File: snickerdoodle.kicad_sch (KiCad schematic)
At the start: 8 parts, among them P2 TFM-115-01-F-D-A, P3 TFM-120-01-F-D-A

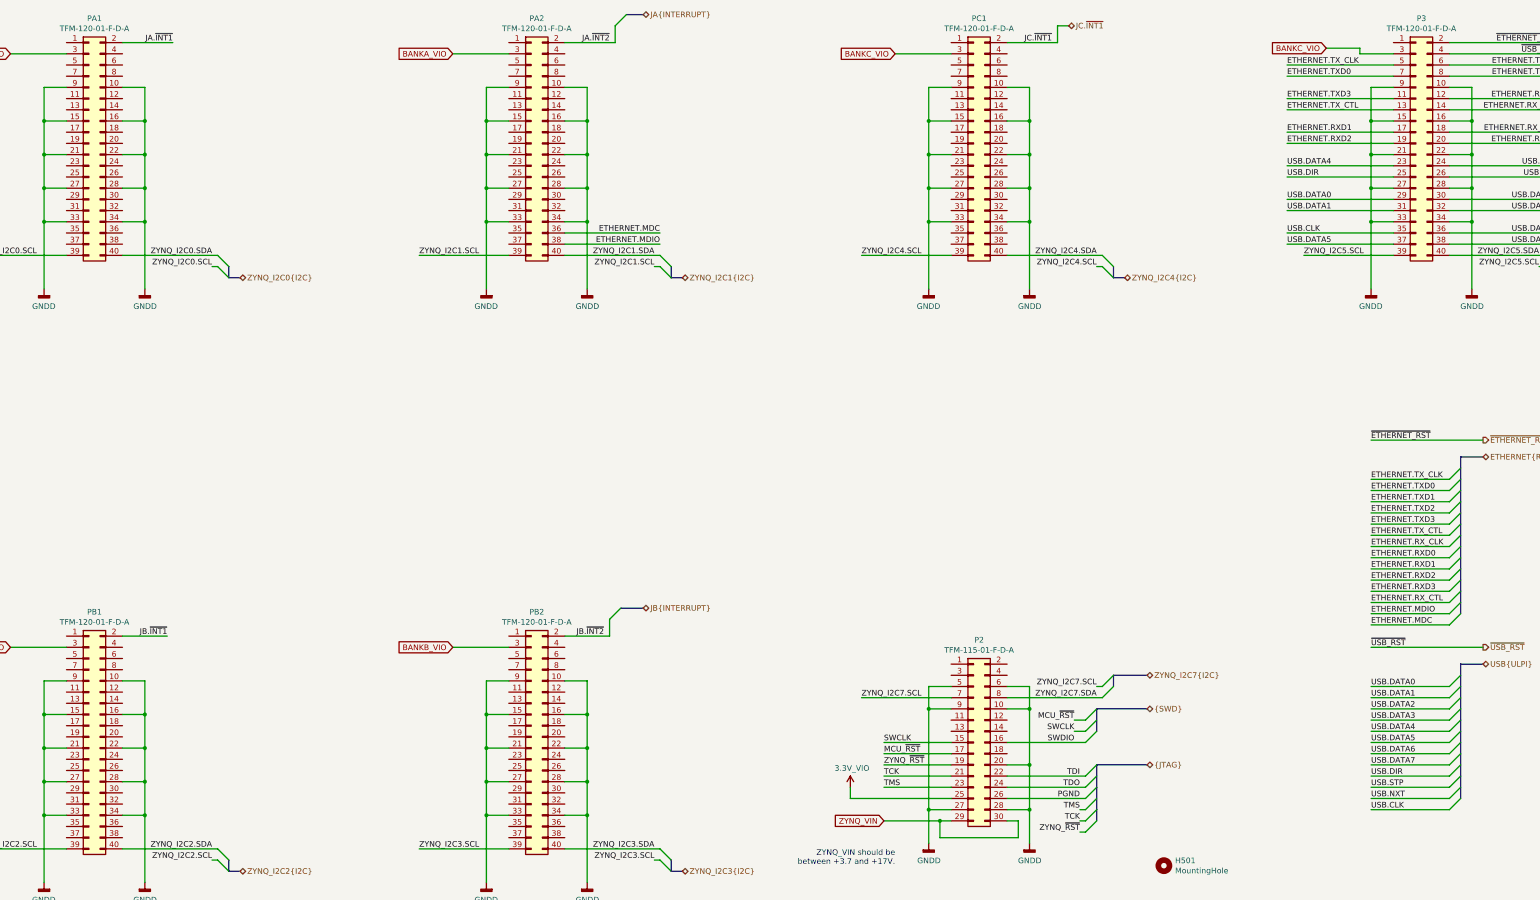
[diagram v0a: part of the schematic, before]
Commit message: Place motor drivers, start layout of Ethernet PHY
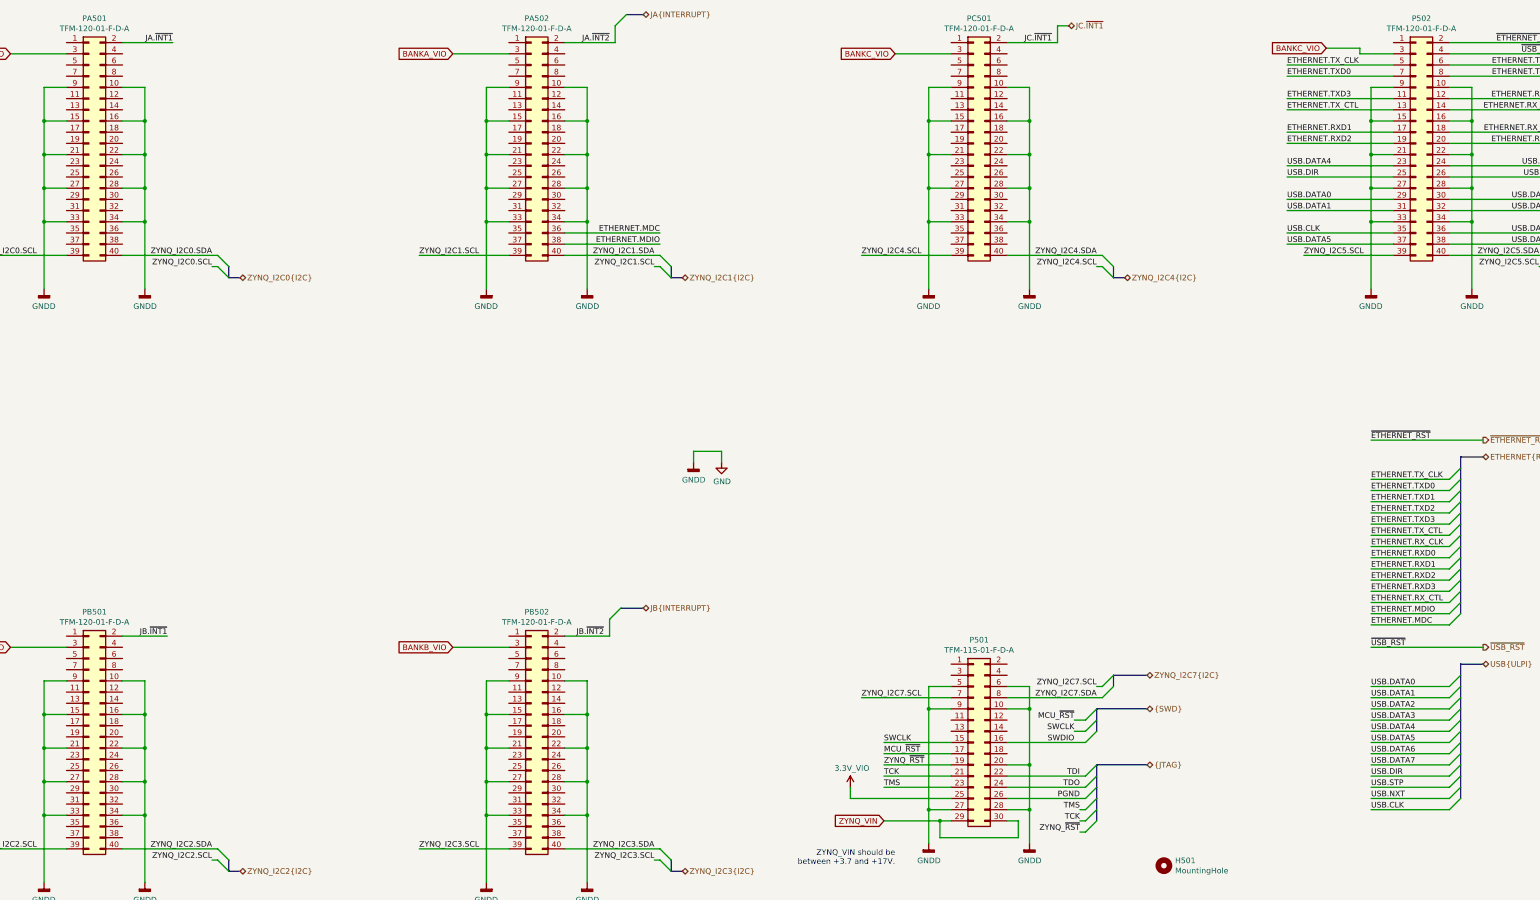
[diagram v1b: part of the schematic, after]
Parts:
- renumbered P2 to P501, P3 to P502, PA1 to PA501, PA2 to PA502, PB1 to PB501, PB2 to PB502, PC1 to PC501
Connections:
- net GNDD renamed GND
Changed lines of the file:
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@@
-(kicad_sch (version 20200618) (host eeschema "5.99.0-unknown-77313e4~101~ubuntu20.04.1")
+(kicad_sch (version 20200618) (host eeschema "5.99.0-unknown-7340c97~102~ubuntu20.04.1")
   (page 5 14)
   (paper "B")
@@
     (comment 1 "Drawn by: Cameron McQuinn")
   )
+  (bus_alias "INTERRUPT" (members "~INT1" "~INT2"))
+  (bus_alias "JTAG" (members "TDI" "TDO" "TCK" "TMS" "ZYNQ_~RST" "PGND"))
+  (bus_alias "I2C" (members "SDA" "SCL"))
   (bus_alias "SWD" (members "MCU_~RST" "SWCLK" "SWDIO"))
-  (bus_alias "I2C" (members "SDA" "SCL"))
-  (bus_alias "JTAG" (members "TDI" "TDO" "TCK" "TMS" "ZYNQ_~RST" "PGND"))
-  (bus_alias "INTERRUPT" (members "~INT1" "~INT2"))
   (junction (at 48.26 45.72) (diameter 0) (color 0 0 0 0))
   (junction (at 48.26 53.34) (diameter 0) (color 0 0 0 0))
@@
     (stroke (width 0) (type solid) (color 0 0 0 0))
   )
+  (wire (pts (xy 195.58 120.65) (xy 195.58 123.19))
+    (stroke (width 0) (type solid) (color 0 0 0 0))
+  )
+  (wire (pts (xy 201.93 120.65) (xy 195.58 120.65))
+    (stroke (width 0) (type solid) (color 0 0 0 0))
+  )
+  (wire (pts (xy 201.93 123.19) (xy 201.93 120.65))
+    (stroke (width 0) (type solid) (color 0 0 0 0))
+  )
   (wire (pts (xy 231.14 196.85) (xy 231.14 199.39))
     (stroke (width 0) (type solid) (color 0 0 0 0))
@@
     (stroke (width 0) (type solid) (color 0 0 0 0))
   )
-  (bus (pts (xy 287.02 196.85) (xy 287.02 201.93))
-    (stroke (width 0) (type solid) (color 0 0 0 0))
-  )
-  (bus (pts (xy 287.02 201.93) (xy 287.02 204.47))
+  (bus (pts (xy 287.02 196.85) (xy 287.02 199.39))
+    (stroke (width 0) (type solid) (color 0 0 0 0))
+  )
+  (bus (pts (xy 287.02 199.39) (xy 287.02 204.47))
     (stroke (width 0) (type solid) (color 0 0 0 0))
   )
@@
     (stroke (width 0) (type solid) (color 0 0 0 0))
   )
-  (bus (pts (xy 369.57 142.24) (xy 369.57 147.32))
-    (stroke (width 0) (type solid) (color 0 0 0 0))
-  )
-  (bus (pts (xy 369.57 147.32) (xy 369.57 152.4))
-    (stroke (width 0) (type solid) (color 0 0 0 0))
-  )
-  (bus (pts (xy 369.57 152.4) (xy 369.57 157.48))
+  (bus (pts (xy 369.57 142.24) (xy 369.57 144.78))
+    (stroke (width 0) (type solid) (color 0 0 0 0))
+  )
+  (bus (pts (xy 369.57 144.78) (xy 369.57 149.86))
+    (stroke (width 0) (type solid) (color 0 0 0 0))
+  )
+  (bus (pts (xy 369.57 149.86) (xy 369.57 154.94))
+    (stroke (width 0) (type solid) (color 0 0 0 0))
+  )
+  (bus (pts (xy 369.57 154.94) (xy 369.57 157.48))
     (stroke (width 0) (type solid) (color 0 0 0 0))
   )
@@
   (symbol (lib_id "Snickerdoodle:3.3V_VIO") (at 231.14 196.85 0) (unit 1)
     (in_bom yes) (on_board yes)
-    (property "Reference" "#PWR0510" (id 0) (at 231.14 200.66 0)
+    (property "Reference" "#PWR0509" (id 0) (at 231.14 200.66 0)
       (effects (font (size 1.27 1.27)) hide)
     )
@@
     )
   )
+  (symbol (lib_id "power:GNDD") (at 195.58 123.19 0) (unit 1)
+    (in_bom yes) (on_board yes)
+    (property "Reference" "#PWR?" (id 0) (at 195.58 129.54 0)
+      (effects (font (size 1.27 1.27)) hide)
+    )
+    (property "Value" "GNDD" (id 1) (at 195.6308 127.1334 0))
+    (property "Footprint" "" (id 2) (at 195.58 123.19 0)
+      (effects (font (size 1.27 1.27)) hide)
+    )
+    (property "Datasheet" "" (id 3) (at 195.58 123.19 0)
+      (effects (font (size 1.27 1.27)) hide)
+    )
+  )
   (symbol (lib_id "power:GNDD") (at 248.92 83.82 0) (mirror y) (unit 1)
     (in_bom yes) (on_board yes)
-    (property "Reference" "#PWR0509" (id 0) (at 248.92 90.17 0)
+    (property "Reference" "#PWR0510" (id 0) (at 248.92 90.17 0)
       (effects (font (size 1.27 1.27)) hide)
     )
@@
   (symbol (lib_id "power:GNDD") (at 248.92 209.55 0) (unit 1)
     (in_bom yes) (on_board yes)
-    (property "Reference" "#PWR0512" (id 0) (at 248.92 215.9 0)
+    (property "Reference" "#PWR0511" (id 0) (at 248.92 215.9 0)
       (effects (font (size 1.27 1.27)) hide)
     )
@@
   (symbol (lib_id "power:GNDD") (at 271.78 83.82 0) (unit 1)
     (in_bom yes) (on_board yes)
-    (property "Reference" "#PWR0511" (id 0) (at 271.78 90.17 0)
+    (property "Reference" "#PWR0512" (id 0) (at 271.78 90.17 0)
       (effects (font (size 1.27 1.27)) hide)
     )
@@
     )
   )
+  (symbol (lib_id "power:GND") (at 201.93 123.19 0) (unit 1)
+    (in_bom yes) (on_board yes)
+    (property "Reference" "#PWR?" (id 0) (at 201.93 129.54 0)
+      (effects (font (size 1.27 1.27)) hide)
+    )
+    (property "Value" "GND" (id 1) (at 202.0443 127.5144 0))
+    (property "Footprint" "" (id 2) (at 201.93 123.19 0)
+      (effects (font (size 1.27 1.27)) hide)
+    )
+    (property "Datasheet" "" (id 3) (at 201.93 123.19 0)
+      (effects (font (size 1.27 1.27)) hide)
+    )
+  )
   (symbol (lib_id "Mechanical:MountingHole") (at 302.26 214.63 0) (unit 1)
     (in_bom yes) (on_board yes)
@@
   (symbol (lib_id "Connector_Generic:Conn_02x15_Odd_Even") (at 259.08 186.69 0) (unit 1)
     (in_bom yes) (on_board yes)
-    (property "Reference" "P2" (id 0) (at 260.35 163.4298 0))
+    (property "Reference" "P501" (id 0) (at 260.35 163.4298 0))
     (property "Value" "TFM-115-01-F-D-A" (id 1) (at 260.35 165.7285 0))
     (property "Footprint" "Connector_Samtec_TFM:Samtec_TFM-115-01-F-D-A_2x15_P1.27mm_Horizontal" (id 2) (at 259.08 186.69 0)
@@
   (symbol (lib_id "Connector_Generic:Conn_02x20_Odd_Even") (at 58.42 50.8 0) (unit 1)
     (in_bom yes) (on_board yes)
-    (property "Reference" "PA1" (id 0) (at 59.69 22.46 0))
+    (property "Reference" "PA501" (id 0) (at 59.69 22.46 0))
     (property "Value" "TFM-120-01-F-D-A" (id 1) (at 59.69 24.7585 0))
     (property "Footprint" "Connector_Samtec_TFM:Samtec_TFM-120-01-F-D-A_2x20_P1.27mm_Horizontal" (id 2) (at 58.42 50.8 0)
@@
   (symbol (lib_id "Connector_Generic:Conn_02x20_Odd_Even") (at 58.42 185.42 0) (unit 1)
     (in_bom yes) (on_board yes)
-    (property "Reference" "PB1" (id 0) (at 59.69 157.08 0))
+    (property "Reference" "PB501" (id 0) (at 59.69 157.08 0))
     (property "Value" "TFM-120-01-F-D-A" (id 1) (at 59.69 159.3785 0))
     (property "Footprint" "Connector_Samtec_TFM:Samtec_TFM-120-01-F-D-A_2x20_P1.27mm_Horizontal" (id 2) (at 58.42 185.42 0)
@@
   (symbol (lib_id "Connector_Generic:Conn_02x20_Odd_Even") (at 158.75 50.8 0) (unit 1)
     (in_bom yes) (on_board yes)
-    (property "Reference" "PA2" (id 0) (at 160.02 22.46 0))
+    (property "Reference" "PA502" (id 0) (at 160.02 22.46 0))
     (property "Value" "TFM-120-01-F-D-A" (id 1) (at 160.02 24.7585 0))
     (property "Footprint" "Connector_Samtec_TFM:Samtec_TFM-120-01-F-D-A_2x20_P1.27mm_Horizontal" (id 2) (at 158.75 50.8 0)
@@
   (symbol (lib_id "Connector_Generic:Conn_02x20_Odd_Even") (at 158.75 185.42 0) (unit 1)
     (in_bom yes) (on_board yes)
-    (property "Reference" "PB2" (id 0) (at 160.02 157.08 0))
+    (property "Reference" "PB502" (id 0) (at 160.02 157.08 0))
     (property "Value" "TFM-120-01-F-D-A" (id 1) (at 160.02 159.3785 0))
     (property "Footprint" "Connector_Samtec_TFM:Samtec_TFM-120-01-F-D-A_2x20_P1.27mm_Horizontal" (id 2) (at 158.75 185.42 0)
@@
   (symbol (lib_id "Connector_Generic:Conn_02x20_Odd_Even") (at 259.08 50.8 0) (unit 1)
     (in_bom yes) (on_board yes)
-    (property "Reference" "PC1" (id 0) (at 260.35 22.46 0))
+    (property "Reference" "PC501" (id 0) (at 260.35 22.46 0))
     (property "Value" "TFM-120-01-F-D-A" (id 1) (at 260.35 24.7585 0))
     (property "Footprint" "Connector_Samtec_TFM:Samtec_TFM-120-01-F-D-A_2x20_P1.27mm_Horizontal" (id 2) (at 259.08 50.8 0)
@@
   (symbol (lib_id "Connector_Generic:Conn_02x20_Odd_Even") (at 359.41 50.8 0) (unit 1)
     (in_bom yes) (on_board yes)
-    (property "Reference" "P3" (id 0) (at 360.68 22.46 0))
+    (property "Reference" "P502" (id 0) (at 360.68 22.46 0))
     (property "Value" "TFM-120-01-F-D-A" (id 1) (at 360.68 24.7585 0))
     (property "Footprint" "Connector_Samtec_TFM:Samtec_TFM-120-01-F-D-A_2x20_P1.27mm_Horizontal" (id 2) (at 359.41 50.8 0)

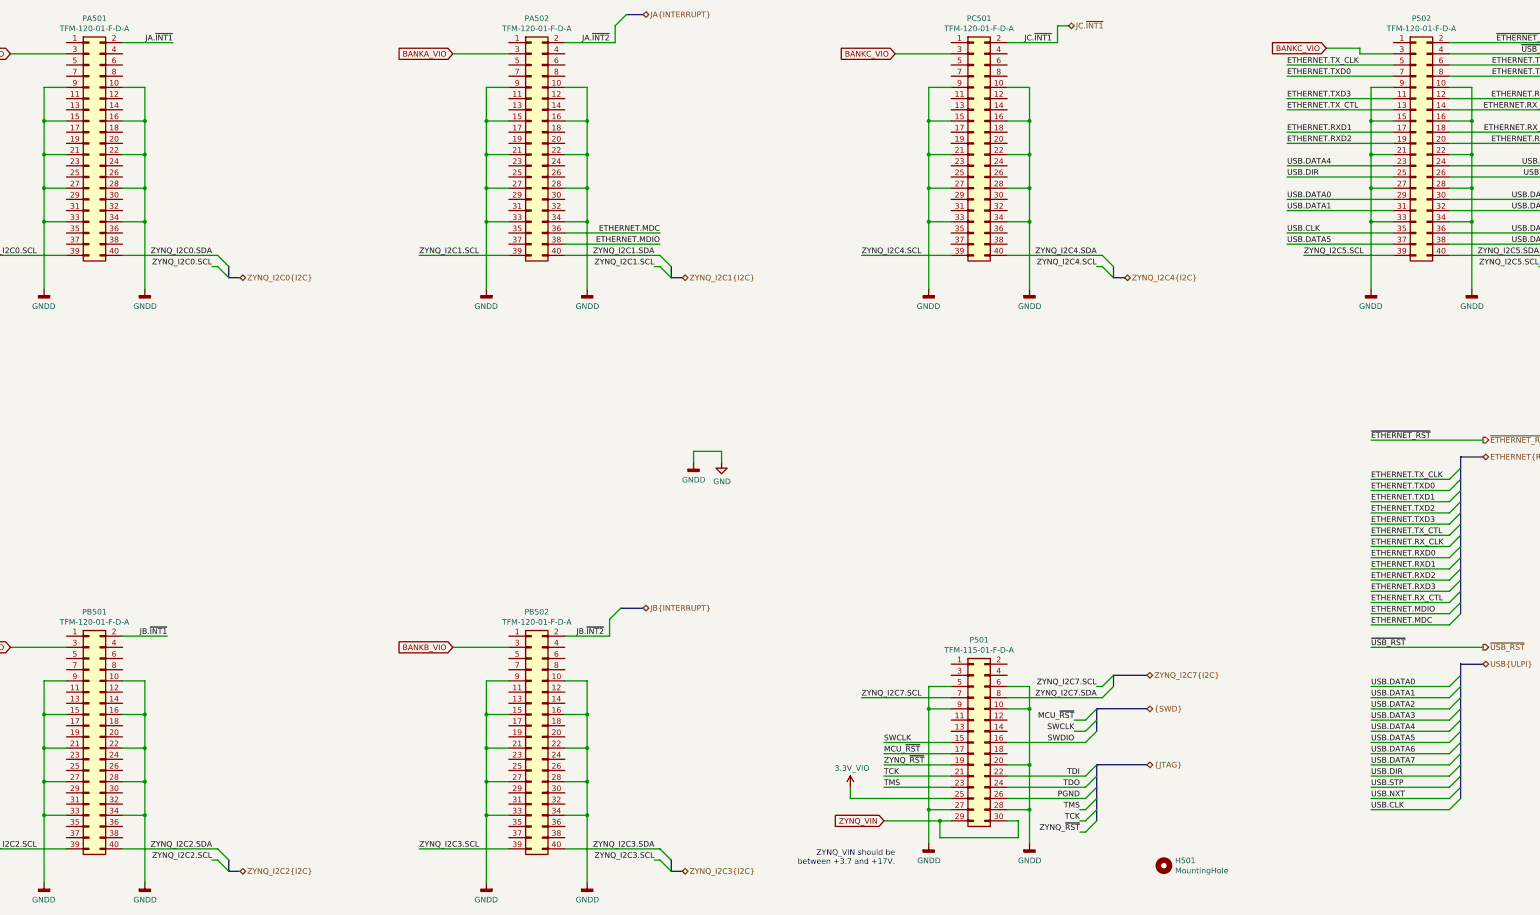
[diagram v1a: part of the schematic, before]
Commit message: Add FTDI chip
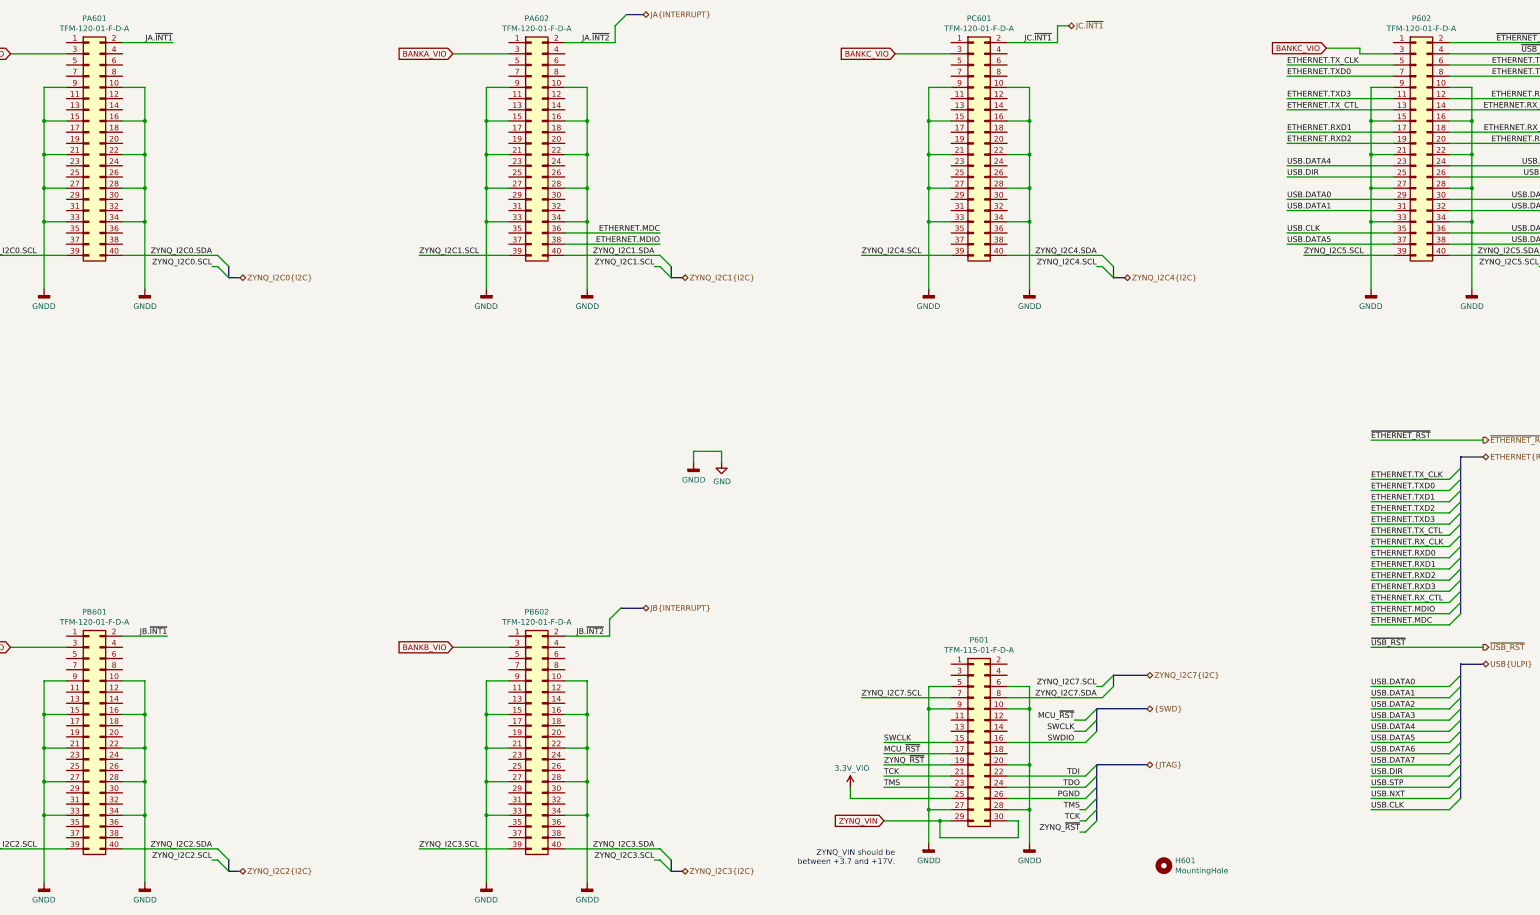
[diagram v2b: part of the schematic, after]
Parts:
- renumbered H501 to H601, P501 to P601, P502 to P602, PA501 to PA601, PA502 to PA602, PB501 to PB601, PB502 to PB602, PC501 to PC601

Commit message: Connect Ethernet PHY to FPGA, route RGMII signals
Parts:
- added C601, C602: 0.1u, Capacitor_SMD:C_0603_1608Metric, symbol Device:C_Small
- added U601: TCA9800, Package_SO:VSSOP-8_3.0x3.0mm_P0.65mm, symbol Interface:TCA9800
- renumbered P601 to J2, P602 to J3, PA601 to JA1, PA602 to JA2, PB601 to JB1, PB602 to JB2, PC601 to JC1
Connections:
- net ETHERNET.MDC: now also JA2.19 (Pin_19); no longer JA2.36 (Pin_36)
- net ETHERNET.MDIO: now also JA2.17 (Pin_17); no longer JA2.38 (Pin_38)
- net ETHERNET.RXD0: now also JA2.30 (Pin_30); no longer J3.12 (Pin_12)
- net ETHERNET.RXD1: now also JA2.26 (Pin_26); no longer J3.17 (Pin_17)
- net ETHERNET.RXD2: now also JA2.24 (Pin_24); no longer J3.19 (Pin_19)
- net ETHERNET.RXD3: now also JA2.20 (Pin_20); no longer J3.20 (Pin_20)
- net ETHERNET.RX_CLK: now also JA2.36 (Pin_36); no longer J3.14 (Pin_14)
- net ETHERNET.RX_CTL: now also JA2.32 (Pin_32); no longer J3.18 (Pin_18)
- net ETHERNET.TXD0: now also JA2.4 (Pin_4); no longer J3.7 (Pin_7)
- net ETHERNET.TXD1: now also JA2.6 (Pin_6); no longer J3.8 (Pin_8)
- net ETHERNET.TXD2: now also JA2.8 (Pin_8); no longer J3.6 (Pin_6)
- net ETHERNET.TXD3: now also JA2.12 (Pin_12); no longer J3.11 (Pin_11)
- net ETHERNET.TX_CLK: now also JA2.14 (Pin_14); no longer J3.5 (Pin_5)
- net ETHERNET.TX_CTL: now also JA2.18 (Pin_18); no longer J3.13 (Pin_13)
- net GND: now also C601.1, C602.1, U601.4 (GND)
- net ~ETHERNET_RST: now also JA2.38 (Pin_38); no longer J3.2 (Pin_2)
- net ~USB_RST: no longer J3.4 (Pin_4)
- net ZYNQ_I2C0.SCL renamed SMB_I2C0.SCL
- net ZYNQ_I2C0.SDA renamed SMB_I2C0.SDA
- net ZYNQ_I2C1.SCL renamed SMB_I2C1.SCL
- net ZYNQ_I2C1.SDA renamed SMB_I2C1.SDA
- net ZYNQ_I2C2.SCL renamed SMB_I2C2.SCL
- net ZYNQ_I2C2.SDA renamed SMB_I2C2.SDA
- net ZYNQ_I2C3.SCL renamed SMB_I2C3.SCL
- net ZYNQ_I2C3.SDA renamed SMB_I2C3.SDA
- net ZYNQ_I2C4.SCL renamed SMB_I2C4.SCL
- net ZYNQ_I2C4.SDA renamed SMB_I2C4.SDA
- net ZYNQ_I2C5.SCL renamed SMB_I2C5.SCL
- net ZYNQ_I2C5.SDA renamed SMB_I2C5.SDA
- net ZYNQ_I2C7.SCL renamed SMB_I2C7.SCL
- net ZYNQ_I2C7.SDA renamed SMB_I2C7.SDA
- new net +1V8: C601.2, U601.1 (VCCA)
- new net +3V3: C602.2, U601.8 (VCCB)
- new net SCK: J3.6 (Pin_6)
- new net SCL: J3.8 (Pin_8), U601.2 (SCLA)
- new net SDA: U601.3 (SDAA)
- new net ZYNQ_I2C.SCL: U601.7 (SCLB)
- new net ZYNQ_I2C.SDA: U601.6 (SDAB)
